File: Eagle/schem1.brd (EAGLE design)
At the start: 125.7 x 77.1 mm, 14 parts, among them X4 RJ45-6L2-B

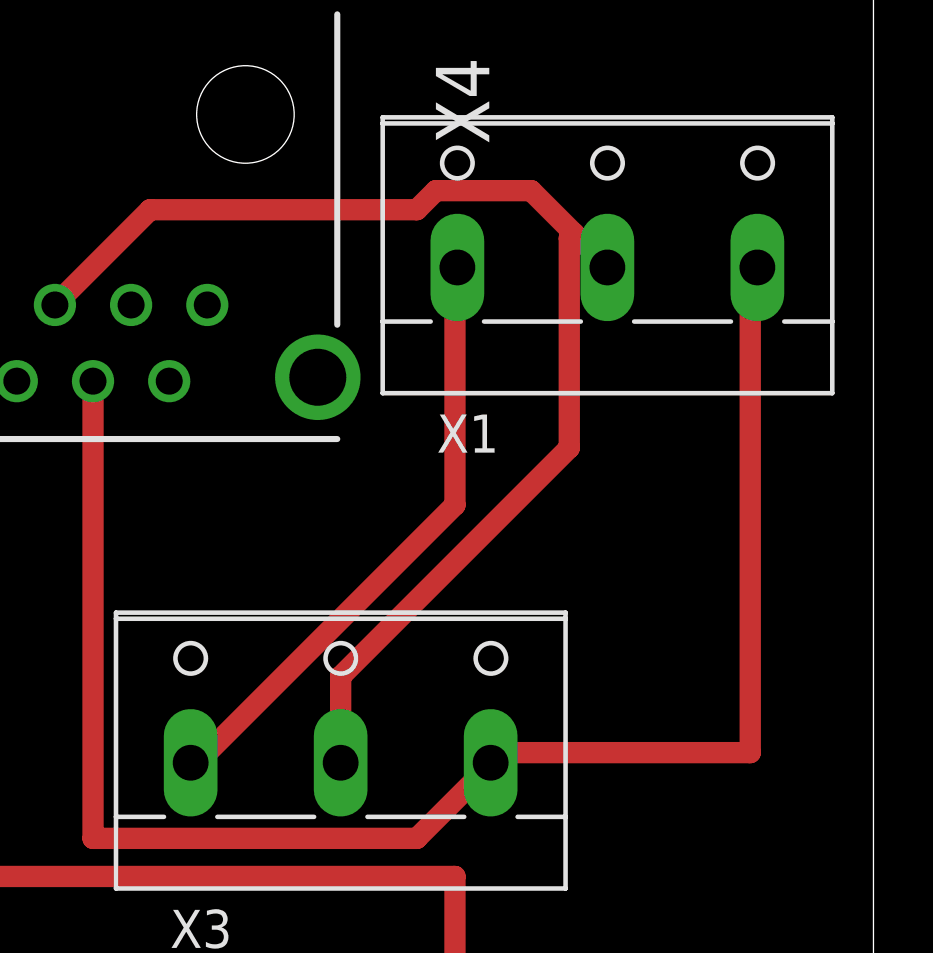
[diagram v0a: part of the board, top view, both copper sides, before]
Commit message: Fixed some Issues with the PCB
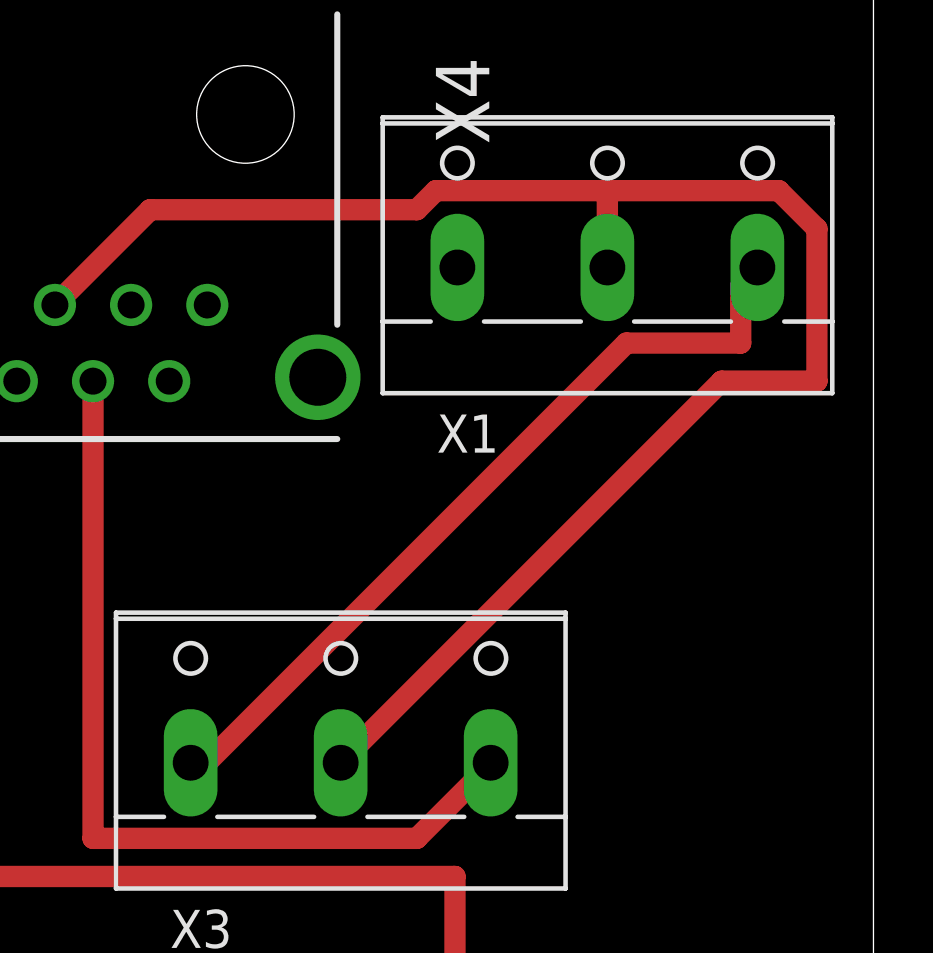
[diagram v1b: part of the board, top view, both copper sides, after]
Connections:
- new net N$3: X1.1
- net A+: no longer X1.3
- net EARTH: now also X1.3; no longer X1.1
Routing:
- net A+: track 54.7 -> 29.9 mm
- net B-: track 41.9 -> 56.3 mm
- net EARTH: track 20.3 -> 27.1 mm
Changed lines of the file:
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@@
 <layer number="14" name="Route14" color="22" fill="1" visible="no" active="no"/>
 <layer number="15" name="Route15" color="23" fill="1" visible="no" active="no"/>
-<layer number="16" name="Bottom" color="1" fill="1" visible="no" active="yes"/>
+<layer number="16" name="Bottom" color="1" fill="1" visible="yes" active="yes"/>
 <layer number="17" name="Pads" color="2" fill="1" visible="yes" active="yes"/>
 <layer number="18" name="Vias" color="2" fill="1" visible="yes" active="yes"/>
 <layer number="19" name="Unrouted" color="6" fill="1" visible="yes" active="yes"/>
-<layer number="20" name="Dimension" color="24" fill="1" visible="no" active="yes"/>
-<layer number="21" name="tPlace" color="7" fill="1" visible="no" active="yes"/>
-<layer number="22" name="bPlace" color="7" fill="1" visible="no" active="yes"/>
-<layer number="23" name="tOrigins" color="15" fill="1" visible="no" active="yes"/>
-<layer number="24" name="bOrigins" color="15" fill="1" visible="no" active="yes"/>
-<layer number="25" name="tNames" color="7" fill="1" visible="no" active="yes"/>
-<layer number="26" name="bNames" color="7" fill="1" visible="no" active="yes"/>
+<layer number="20" name="Dimension" color="24" fill="1" visible="yes" active="yes"/>
+<layer number="21" name="tPlace" color="7" fill="1" visible="yes" active="yes"/>
+<layer number="22" name="bPlace" color="7" fill="1" visible="yes" active="yes"/>
+<layer number="23" name="tOrigins" color="15" fill="1" visible="yes" active="yes"/>
+<layer number="24" name="bOrigins" color="15" fill="1" visible="yes" active="yes"/>
+<layer number="25" name="tNames" color="7" fill="1" visible="yes" active="yes"/>
+<layer number="26" name="bNames" color="7" fill="1" visible="yes" active="yes"/>
 <layer number="27" name="tValues" color="7" fill="1" visible="no" active="yes"/>
 <layer number="28" name="bValues" color="7" fill="1" visible="no" active="yes"/>
@@
 <layer number="37" name="tTest" color="7" fill="1" visible="no" active="yes"/>
 <layer number="38" name="bTest" color="7" fill="1" visible="no" active="yes"/>
-<layer number="39" name="tKeepout" color="4" fill="11" visible="no" active="yes"/>
-<layer number="40" name="bKeepout" color="1" fill="11" visible="no" active="yes"/>
-<layer number="41" name="tRestrict" color="4" fill="10" visible="no" active="yes"/>
-<layer number="42" name="bRestrict" color="1" fill="10" visible="no" active="yes"/>
+<layer number="39" name="tKeepout" color="4" fill="11" visible="yes" active="yes"/>
+<layer number="40" name="bKeepout" color="1" fill="11" visible="yes" active="yes"/>
+<layer number="41" name="tRestrict" color="4" fill="10" visible="yes" active="yes"/>
+<layer number="42" name="bRestrict" color="1" fill="10" visible="yes" active="yes"/>
 <layer number="43" name="vRestrict" color="2" fill="10" visible="no" active="yes"/>
 <layer number="44" name="Drills" color="7" fill="1" visible="no" active="yes"/>
@@
 <layer number="49" name="Reference" color="7" fill="1" visible="no" active="yes"/>
 <layer number="50" name="dxf" color="7" fill="1" visible="no" active="no"/>
-<layer number="51" name="tDocu" color="7" fill="1" visible="no" active="yes"/>
-<layer number="52" name="bDocu" color="7" fill="1" visible="no" active="yes"/>
+<layer number="51" name="tDocu" color="7" fill="1" visible="yes" active="yes"/>
+<layer number="52" name="bDocu" color="7" fill="1" visible="yes" active="yes"/>
 <layer number="53" name="tGND_GNDA" color="7" fill="9" visible="no" active="no"/>
 <layer number="54" name="bGND_GNDA" color="1" fill="9" visible="no" active="no"/>
@@
 <autorouter>
 <pass name="Default">
-<param name="RoutingGrid" value="50mil"/>
+<param name="RoutingGrid" value="25mil"/>
 <param name="AutoGrid" value="1"/>
 <param name="Efforts" value="0"/>
 <param name="TopRouterVariant" value="1"/>
 <param name="tpViaShape" value="round"/>
-<param name="PrefDir.1" value="a"/>
+<param name="PrefDir.1" value="|"/>
 <param name="PrefDir.2" value="0"/>
 <param name="PrefDir.3" value="0"/>
@@
 <wire x1="143.51" y1="3.81" x2="143.51" y2="4.1275" width="0.7112" layer="1"/>
 </signal>
+<signal name="N$3">
+<contactref element="X1" pad="1"/>
+</signal>
 <signal name="A+">
 <contactref element="X3" pad="3"/>
-<contactref element="X1" pad="3"/>
 <contactref element="X4" pad="4"/>
 <wire x1="133.985" y1="41.91" x2="133.985" y2="57.15" width="0.7112" layer="1"/>
@@
 <wire x1="147.0025" y1="44.1325" x2="144.78" y2="41.91" width="0.7112" layer="1"/>
 <wire x1="147.0025" y1="44.1325" x2="147.24" y2="44.43" width="0.7112" layer="1"/>
-<wire x1="155.8925" y1="44.7675" x2="155.8925" y2="60.6425" width="0.7112" layer="1"/>
-<wire x1="147.32" y1="44.7675" x2="155.8925" y2="44.7675" width="0.7112" layer="1"/>
-<wire x1="155.8925" y1="60.6425" x2="156.13" y2="60.94" width="0.7112" layer="1"/>
 <wire x1="147.32" y1="44.7675" x2="147.24" y2="44.43" width="0.7112" layer="1"/>
 </signal>
 <signal name="B-">
 <contactref element="X3" pad="2"/>
+<contactref element="X4" pad="5"/>
 <contactref element="X1" pad="2"/>
-<contactref element="X4" pad="5"/>
 <wire x1="135.89" y1="62.865" x2="132.715" y2="59.69" width="0.7112" layer="1"/>
 <wire x1="144.78" y1="62.865" x2="135.89" y2="62.865" width="0.7112" layer="1"/>
 <wire x1="145.415" y1="63.5" x2="144.78" y2="62.865" width="0.7112" layer="1"/>
-<wire x1="148.59" y1="63.5" x2="145.415" y2="63.5" width="0.7112" layer="1"/>
-<wire x1="151.13" y1="60.96" x2="150.01875" y2="62.07125" width="0.7112" layer="1"/>
-<wire x1="150.01875" y1="62.07125" x2="148.59" y2="63.5" width="0.7112" layer="1"/>
-<wire x1="151.13" y1="60.96" x2="151.13" y2="60.94" width="0.7112" layer="1"/>
-<wire x1="142.24" y1="47.3075" x2="142.24" y2="44.43" width="0.7112" layer="1"/>
-<wire x1="149.86" y1="54.9275" x2="142.24" y2="47.3075" width="0.7112" layer="1"/>
-<wire x1="149.86" y1="61.9125" x2="149.86" y2="54.9275" width="0.7112" layer="1"/>
-<wire x1="149.86" y1="61.9125" x2="150.01875" y2="62.07125" width="0.7112" layer="1"/>
+<wire x1="151.13" y1="63.5" x2="145.415" y2="63.5" width="0.7112" layer="1"/>
+<wire x1="151.13" y1="60.94" x2="151.13" y2="63.5" width="0.7112" layer="1"/>
+<wire x1="154.94" y1="57.15" x2="142.24" y2="44.45" width="0.7112" layer="1"/>
+<wire x1="158.115" y1="57.15" x2="154.94" y2="57.15" width="0.7112" layer="1"/>
+<wire x1="158.115" y1="62.23" x2="158.115" y2="57.15" width="0.7112" layer="1"/>
+<wire x1="156.845" y1="63.5" x2="158.115" y2="62.23" width="0.7112" layer="1"/>
+<wire x1="151.13" y1="63.5" x2="156.845" y2="63.5" width="0.7112" layer="1"/>
+<wire x1="142.24" y1="44.45" x2="142.24" y2="44.43" width="0.7112" layer="1"/>
 </signal>
 <signal name="EARTH">
 <contactref element="X3" pad="1"/>
-<contactref element="X1" pad="1"/>
-<wire x1="146.05" y1="53.0225" x2="137.4775" y2="44.45" width="0.7112" layer="1"/>
-<wire x1="146.05" y1="60.6425" x2="146.05" y2="53.0225" width="0.7112" layer="1"/>
 <wire x1="137.4775" y1="44.45" x2="137.24" y2="44.43" width="0.7112" layer="1"/>
-<wire x1="146.05" y1="60.6425" x2="146.13" y2="60.94" width="0.7112" layer="1"/>
+<contactref element="X1" pad="3"/>
+<wire x1="151.765" y1="58.42" x2="137.795" y2="44.45" width="0.7112" layer="1"/>
+<wire x1="155.575" y1="58.42" x2="151.765" y2="58.42" width="0.7112" layer="1"/>
+<wire x1="155.575" y1="60.325" x2="155.575" y2="58.42" width="0.7112" layer="1"/>
+<wire x1="137.795" y1="44.45" x2="137.24" y2="44.43" width="0.7112" layer="1"/>
+<wire x1="155.575" y1="60.325" x2="156.13" y2="60.94" width="0.7112" layer="1"/>
 </signal>
 <signal name="SCL">
